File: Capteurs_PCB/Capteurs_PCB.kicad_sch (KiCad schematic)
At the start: 0 parts

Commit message: update kicad
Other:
- sheet Regulation 5V renamed Regulation
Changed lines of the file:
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@@
     (stroke (width 0.1524) (type solid))
     (fill (color 0 0 0 0.0000))
-    (property "Sheetname" "Regulation 5V" (at 25.4 72.9484 0)
+    (property "Sheetname" "Regulation" (at 25.4 72.9484 0)
       (effects (font (size 1.27 1.27)) (justify left bottom))
     )

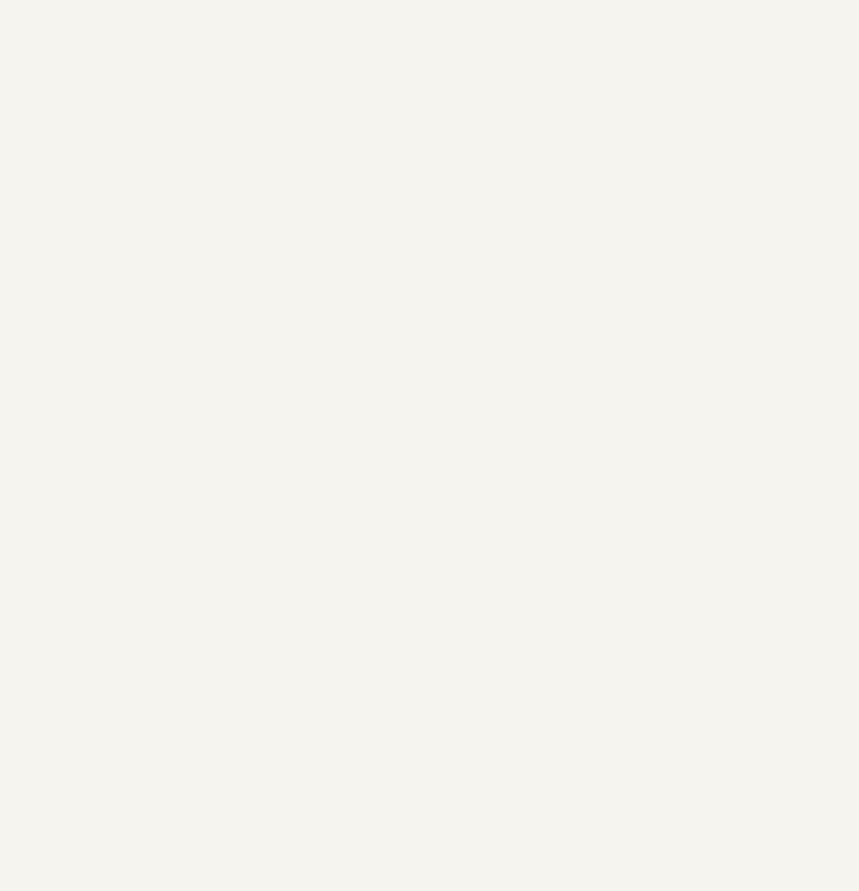
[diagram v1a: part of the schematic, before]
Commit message: PCB changement
Pcb changé (Raspberry))
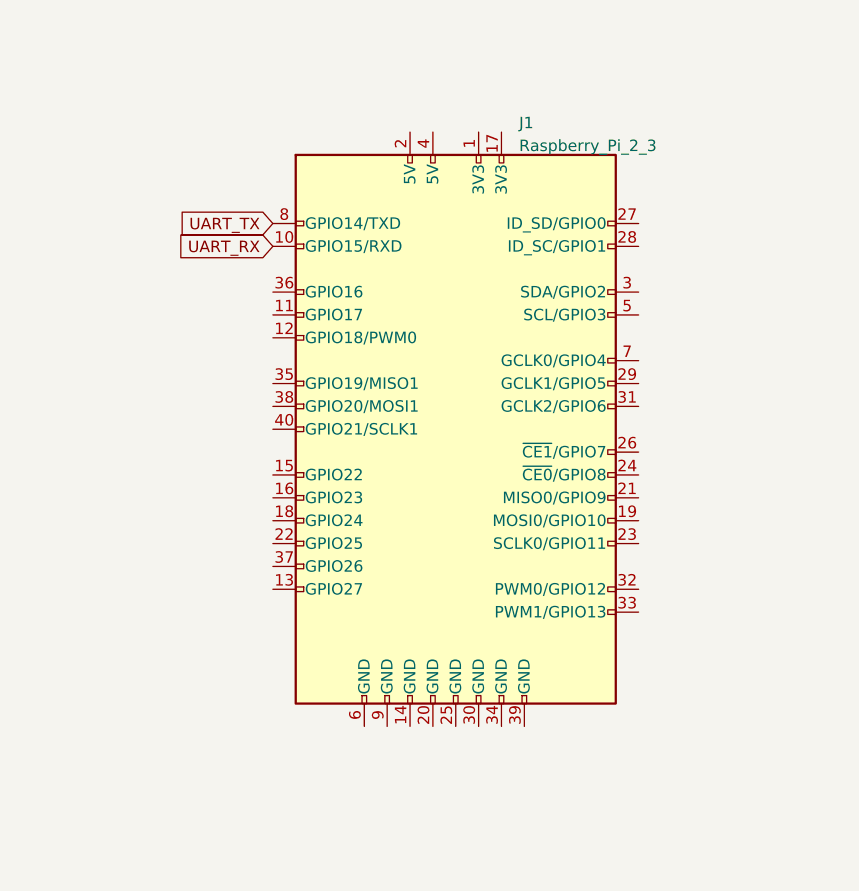
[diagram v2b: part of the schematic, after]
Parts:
- added J1: Raspberry_Pi_2_3, symbol Connector:Raspberry_Pi_2_3
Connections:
- new net UART_RX: J1.10 (GPIO15/RXD)
- new net UART_TX: J1.8 (GPIO14/TXD)
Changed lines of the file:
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@@
     (title "PCB_CAPTEUR_ALIM")
+  )
+  (global_label "UART_TX" (shape input) (at 105.156 42.926 180) (fields_autoplaced)
+    (effects (font (size 1.27 1.27)) (justify right))
+    (property "Intersheetrefs" "${INTERSHEET_REFS}" (at 94.4488 42.926 0)
+      (effects (font (size 1.27 1.27)) (justify right) hide)
+    )
+  )
+  (global_label "UART_RX" (shape input) (at 105.156 45.466 180) (fields_autoplaced)
+    (effects (font (size 1.27 1.27)) (justify right))
+    (property "Intersheetrefs" "${INTERSHEET_REFS}" (at 94.1464 45.466 0)
+      (effects (font (size 1.27 1.27)) (justify right) hide)
+    )
+  )
+  (symbol (lib_id "Connector:Raspberry_Pi_2_3") (at 125.476 65.786 0) (unit 1)
+    (in_bom yes) (on_board yes) (dnp no) (fields_autoplaced)
+    (property "Reference" "J1" (at 132.5119 31.75 0)
+      (effects (font (size 1.27 1.27)) (justify left))
+    )
+    (property "Value" "Raspberry_Pi_2_3" (at 132.5119 34.29 0)
+      (effects (font (size 1.27 1.27)) (justify left))
+    )
+    (property "Footprint" "" (at 125.476 65.786 0)
+      (effects (font (size 1.27 1.27)) hide)
+    )
+    (property "Datasheet" "https://www.raspberrypi.org/documentation/hardware/raspberrypi/schematics/rpi_SCH_3bplus_1p0_reduced.pdf" (at 125.476 65.786 0)
+      (effects (font (size 1.27 1.27)) hide)
+    )
+    (pin "1")
+    (pin "10")
+    (pin "11")
+    (pin "12")
+    (pin "13")
+    (pin "14")
+    (pin "15")
+    (pin "16")
+    (pin "17")
+    (pin "18")
+    (pin "19")
+    (pin "2")
+    (pin "20")
+    (pin "21")
+    (pin "22")
+    (pin "23")
+    (pin "24")
+    (pin "25")
+    (pin "26")
+    (pin "27")
+    (pin "28")
+    (pin "29")
+    (pin "3")
+    (pin "30")
+    (pin "31")
+    (pin "32")
+    (pin "33")
+    (pin "34")
+    (pin "35")
+    (pin "36")
+    (pin "37")
+    (pin "38")
+    (pin "39")
+    (pin "4")
+    (pin "40")
+    (pin "5")
+    (pin "6")
+    (pin "7")
+    (pin "8")
+    (pin "9")
+    (instances
+      (project "Capteurs_PCB"
+        (path "/1101af8f-9425-4102-9245-339dc54562bf"
+          (reference "J1") (unit 1)
+        )
+      )
+    )
   )
   (sheet (at 24.13 130.81) (size 64.77 53.34) (fields_autoplaced)

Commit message: pcb update
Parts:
- removed J1: Raspberry_Pi_2_3, symbol Connector:Raspberry_Pi_2_3
- added J1: Batterie, symbol Connector:Conn_01x02_Socket
- added J2: RaspberryPi, symbol Connector:Conn_01x02_Socket
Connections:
- net UART_RX: now also J2.2 (Pin_2)
- net UART_TX: now also J2.1 (Pin_1)
- new net Earth: J1.1 (Pin_1)
- new net VBATTERIE: J1.2 (Pin_2)
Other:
- note added: "Batterie"
- note added: "Branchement RaspberryPi"

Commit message: uptdate PCB
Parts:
- added J3: Prop1, symbol Connector:Conn_01x03_Pin
- added J4: Prop2, symbol Connector:Conn_01x03_Pin
- added J5: Alim_Prop1, symbol Connector:Conn_01x02_Socket
- added J6: Alim_Prop2, symbol Connector:Conn_01x02_Socket
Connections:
- net Earth: now also J3.3 (Pin_3), J4.3 (Pin_3), J5.2 (Pin_2), J6.2 (Pin_2)
- new net 5_V5: J3.2 (Pin_2), J4.2 (Pin_2)
- new net SigProp1: J3.1 (Pin_1)
- new net SigProp2: J4.1 (Pin_1)
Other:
- note added: "Propulseurs"
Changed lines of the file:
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@@
   (junction (at 64.77 81.28) (diameter 0) (color 0 0 0 0)
   )
+  (junction (at 91.44 74.93) (diameter 0) (color 0 0 0 0)
+  )
   (junction (at 111.76 128.27) (diameter 0) (color 0 0 0 0)
   )
@@
     (stroke (width 0) (type default))
   )
+  (wire (pts (xy 91.44 74.93) (xy 91.44 77.47))
+    (stroke (width 0) (type default))
+  )
+  (wire (pts (xy 87.63 77.47) (xy 87.63 74.93))
+    (stroke (width 0) (type default))
+  )
   (wire (pts (xy 104.14 132.08) (xy 116.84 132.08))
     (stroke (width 0) (type default))
@@
     (stroke (width 0) (type default))
   )
+  (wire (pts (xy 87.63 74.93) (xy 91.44 74.93))
+    (stroke (width 0) (type default))
+  )
   (wire (pts (xy 104.14 96.52) (xy 116.84 96.52))
     (stroke (width 0) (type default))
@@
     (stroke (width 0) (type default))
   )
-  (wire (pts (xy 91.44 67.31) (xy 91.44 77.47))
+  (wire (pts (xy 91.44 67.31) (xy 91.44 74.93))
     (stroke (width 0) (type default))
   )
@@
   (wire (pts (xy 64.77 81.28) (xy 64.77 67.31))
     (stroke (width 0) (type default))
+  )
+  (rectangle (start 212.09 45.72) (end 265.43 96.52)
+    (stroke (width 0) (type default))
+    (fill (type none))
   )
   (rectangle (start 63.5 24.13) (end 90.17 52.07)
@@
     (effects (font (size 1.27 1.27)) (justify left bottom))
   )
+  (text "Propulseurs\n" (at 212.09 45.72 0)
+    (effects (font (size 1.27 1.27)) (justify left bottom))
+  )
   (global_label "V_5V" (shape input) (at 53.34 85.09 180) (fields_autoplaced)
     (effects (font (size 1.27 1.27)) (justify right))
@@
     )
   )
+  (global_label "SigProp1" (shape input) (at 226.06 57.15 180) (fields_autoplaced)
+    (effects (font (size 1.27 1.27)) (justify right))
+    (property "Intersheetrefs" "${INTERSHEET_REFS}" (at 214.6272 57.15 0)
+      (effects (font (size 1.27 1.27)) (justify right) hide)
+    )
+  )
   (global_label "SDX" (shape input) (at 116.84 87.63 0) (fields_autoplaced)
     (effects (font (size 1.27 1.27)) (justify left))
@@
     )
   )
+  (global_label "5_V5" (shape input) (at 226.06 54.61 180) (fields_autoplaced)
+    (effects (font (size 1.27 1.27)) (justify right))
+    (property "Intersheetrefs" "${INTERSHEET_REFS}" (at 218.679 54.61 0)
+      (effects (font (size 1.27 1.27)) (justify right) hide)
+    )
+  )
   (global_label "INT2" (shape input) (at 104.14 99.06 180) (fields_autoplaced)
     (effects (font (size 1.27 1.27)) (justify right))
@@
     )
   )
+  (global_label "SigProp2" (shape input) (at 226.06 67.31 180) (fields_autoplaced)
+    (effects (font (size 1.27 1.27)) (justify right))
+    (property "Intersheetrefs" "${INTERSHEET_REFS}" (at 214.6272 67.31 0)
+      (effects (font (size 1.27 1.27)) (justify right) hide)
+    )
+  )
   (global_label "CS" (shape input) (at 116.84 90.17 0) (fields_autoplaced)
     (effects (font (size 1.27 1.27)) (justify left))
@@
     )
   )
+  (global_label "5_V5" (shape input) (at 226.06 64.77 180) (fields_autoplaced)
+    (effects (font (size 1.27 1.27)) (justify right))
+    (property "Intersheetrefs" "${INTERSHEET_REFS}" (at 218.679 64.77 0)
+      (effects (font (size 1.27 1.27)) (justify right) hide)
+    )
+  )
   (global_label "SS" (shape input) (at 104.14 139.7 180) (fields_autoplaced)
     (effects (font (size 1.27 1.27)) (justify right))
@@
         (path "/1101af8f-9425-4102-9245-339dc54562bf"
           (reference "J1") (unit 1)
+        )
+      )
+    )
+  )
+  (symbol (lib_id "Connector:Conn_01x02_Socket") (at 231.14 83.82 0) (unit 1)
+    (in_bom yes) (on_board yes) (dnp no)
+    (property "Reference" "J6" (at 231.14 92.71 0)
+      (effects (font (size 1.27 1.27)))
+    )
+    (property "Value" "Alim_Prop2" (at 231.14 90.17 0)
+      (effects (font (size 1.27 1.27)))
+    )
+    (property "Footprint" "" (at 231.14 83.82 0)
+      (effects (font (size 1.27 1.27)) hide)
+    )
+    (property "Datasheet" "~" (at 231.14 83.82 0)
+      (effects (font (size 1.27 1.27)) hide)
+    )
+    (pin "1")
+    (pin "2")
+    (instances
+      (project "Capteurs_PCB"
+        (path "/1101af8f-9425-4102-9245-339dc54562bf"
+          (reference "J6") (unit 1)
+        )
+      )
+    )
+  )
+  (symbol (lib_id "power:Earth") (at 226.06 52.07 270) (unit 1)
+    (in_bom yes) (on_board yes) (dnp no) (fields_autoplaced)
+    (property "Reference" "#PWR09" (at 219.71 52.07 0)
+      (effects (font (size 1.27 1.27)) hide)
+    )
+    (property "Value" "Earth" (at 222.25 52.07 0)
+      (effects (font (size 1.27 1.27)) hide)
+    )
+    (property "Footprint" "" (at 226.06 52.07 0)
+      (effects (font (size 1.27 1.27)) hide)
+    )
+    (property "Datasheet" "~" (at 226.06 52.07 0)
+      (effects (font (size 1.27 1.27)) hide)
+    )
+    (pin "1")
+    (instances
+      (project "Capteurs_PCB"
+        (path "/1101af8f-9425-4102-9245-339dc54562bf"
+          (reference "#PWR09") (unit 1)
         )
       )
@@
     )
   )
+  (symbol (lib_id "power:Earth") (at 226.06 74.93 270) (unit 1)
+    (in_bom yes) (on_board yes) (dnp no) (fields_autoplaced)
+    (property "Reference" "#PWR011" (at 219.71 74.93 0)
+      (effects (font (size 1.27 1.27)) hide)
+    )
+    (property "Value" "Earth" (at 222.25 74.93 0)
+      (effects (font (size 1.27 1.27)) hide)
+    )
+    (property "Footprint" "" (at 226.06 74.93 0)
+      (effects (font (size 1.27 1.27)) hide)
+    )
+    (property "Datasheet" "~" (at 226.06 74.93 0)
+      (effects (font (size 1.27 1.27)) hide)
+    )
+    (pin "1")
+    (instances
+      (project "Capteurs_PCB"
+        (path "/1101af8f-9425-4102-9245-339dc54562bf"
+          (reference "#PWR011") (unit 1)
+        )
+      )
+    )
+  )
+  (symbol (lib_id "Connector:Conn_01x03_Pin") (at 231.14 54.61 180) (unit 1)
+    (in_bom yes) (on_board yes) (dnp no) (fields_autoplaced)
+    (property "Reference" "J3" (at 232.41 53.975 0)
+      (effects (font (size 1.27 1.27)) (justify right))
+    )
+    (property "Value" "Prop1" (at 232.41 56.515 0)
+      (effects (font (size 1.27 1.27)) (justify right))
+    )
+    (property "Footprint" "" (at 231.14 54.61 0)
+      (effects (font (size 1.27 1.27)) hide)
+    )
+    (property "Datasheet" "~" (at 231.14 54.61 0)
+      (effects (font (size 1.27 1.27)) hide)
+    )
+    (pin "1")
+    (pin "2")
+    (pin "3")
+    (instances
+      (project "Capteurs_PCB"
+        (path "/1101af8f-9425-4102-9245-339dc54562bf"
+          (reference "J3") (unit 1)
+        )
+      )
+    )
+  )
+  (symbol (lib_id "power:Earth") (at 226.06 86.36 270) (unit 1)
+    (in_bom yes) (on_board yes) (dnp no) (fields_autoplaced)
+    (property "Reference" "#PWR012" (at 219.71 86.36 0)
+      (effects (font (size 1.27 1.27)) hide)
+    )
+    (property "Value" "Earth" (at 222.25 86.36 0)
+      (effects (font (size 1.27 1.27)) hide)
+    )
+    (property "Footprint" "" (at 226.06 86.36 0)
+      (effects (font (size 1.27 1.27)) hide)
+    )
+    (property "Datasheet" "~" (at 226.06 86.36 0)
+      (effects (font (size 1.27 1.27)) hide)
+    )
+    (pin "1")
+    (instances
+      (project "Capteurs_PCB"
+        (path "/1101af8f-9425-4102-9245-339dc54562bf"
+          (reference "#PWR012") (unit 1)
+        )
+      )
+    )
+  )
   (symbol (lib_id "power:Earth") (at 34.29 55.88 0) (unit 1)
     (in_bom yes) (on_board yes) (dnp no) (fields_autoplaced)
@@
         )
       )
+    )
+  )
+  (symbol (lib_id "power:Earth") (at 226.06 62.23 270) (unit 1)
+    (in_bom yes) (on_board yes) (dnp no) (fields_autoplaced)
+    (property "Reference" "#PWR010" (at 219.71 62.23 0)
+      (effects (font (size 1.27 1.27)) hide)
+    )
+    (property "Value" "Earth" (at 222.25 62.23 0)
+      (effects (font (size 1.27 1.27)) hide)
+    )
+    (property "Footprint" "" (at 226.06 62.23 0)
+      (effects (font (size 1.27 1.27)) hide)
+    )
+    (property "Datasheet" "~" (at 226.06 62.23 0)
+      (effects (font (size 1.27 1.27)) hide)
+    )
+    (pin "1")
+    (instances
+      (project "Capteurs_PCB"
+        (path "/1101af8f-9425-4102-9245-339dc54562bf"
+          (reference "#PWR010") (unit 1)
+        )
+      )
+    )
+  )
+  (symbol (lib_id "Connector:Conn_01x03_Pin") (at 231.14 64.77 180) (unit 1)
+    (in_bom yes) (on_board yes) (dnp no) (fields_autoplaced)
+    (property "Reference" "J4" (at 232.41 64.135 0)
+      (effects (font (size 1.27 1.27)) (justify right))
+    )
+    (property "Value" "Prop2" (at 232.41 66.675 0)
+      (effects (font (size 1.27 1.27)) (justify right))
+    )
+    (property "Footprint" "" (at 231.14 64.77 0)
+      (effects (font (size 1.27 1.27)) hide)
+    )
+    (property "Datasheet" "~" (at 231.14 64.77 0)
+      (effects (font (size 1.27 1.27)) hide)
+    )
+    (pin "1")
+    (pin "2")
+    (pin "3")
+    (instances
+      (project "Capteurs_PCB"
+        (path "/1101af8f-9425-4102-9245-339dc54562bf"
+          (reference "J4") (unit 1)
+        )
+      )
+    )
+  )
+  (symbol (lib_id "Connector:Conn_01x02_Socket") (at 231.14 72.39 0) (unit 1)
+    (in_bom yes) (on_board yes) (dnp no)
+    (property "Reference" "J5" (at 231.14 81.28 0)
+      (effects (font (size 1.27 1.27)))
+    )
+    (property "Value" "Alim_Prop1" (at 231.14 78.74 0)
+      (effects (font (size 1.27 1.27)))
+    )
+    (property "Footprint" "" (at 231.14 72.39 0)
+      (effects (font (size 1.27 1.27)) hide)
+    )
+    (property "Datasheet" "~" (at 231.14 72.39 0)
+      (effects (font (size 1.27 1.27)) hide)
+    )
+    (pin "1")
+    (pin "2")
+    (instances
+      (project "Capteurs_PCB"
+        (path "/1101af8f-9425-4102-9245-339dc54562bf"
+          (reference "J5") (unit 1)
+        )
+      )

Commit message: updates pcb
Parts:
- added J7: Moteur_seringues_1, Connector_PinSocket_2.54mm:PinSocket_1x02_P2.54mm_Vertical, symbol Connector:Conn_01x02_Socket
- added J8: Moteur_seringues_2, Connector_PinSocket_2.54mm:PinSocket_1x02_P2.54mm_Vertical, symbol Connector:Conn_01x02_Socket
- added J9: LED, Connector_PinHeader_2.54mm:PinHeader_1x04_P2.54mm_Vertical, symbol Connector:Conn_01x04_Pin
- added U7, U8: ZXBM5210-SP, Package_SO:Diodes_SO-8EP, symbol Driver_Motor:ZXBM5210-SP
- J2: footprint (none) -> Connector_PinSocket_2.54mm:PinSocket_1x02_P2.54mm_Vertical
- J3, J4: footprint (none) -> Connector_PinHeader_2.54mm:PinHeader_1x03_P2.54mm_Vertical
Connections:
- net Earth: now also J9.2 (Pin_2), J9.4 (Pin_4), U7.8 (GND), U7.9 (GND), U8.8 (GND), U8.9 (GND)
- net V_12V: now also J5.1 (Pin_1), J6.1 (Pin_1), U7.2 (VM), U7.3 (VDD), U7.6 (VREF), U8.2 (VM), U8.3 (VDD), U8.6 (VREF)
- net 5_V5 renamed VDD_LED
- net VDD_LED: now also J9.3 (Pin_3)
- new net: J8.1 (Pin_1), U8.1 (OUT1)
- new net: J8.2 (Pin_2), U8.7 (OUT2)
- new net: J7.1 (Pin_1), U7.1 (OUT1)
- new net: J7.2 (Pin_2), U7.7 (OUT2)
- new net FWD1: U7.4 (FWD)
- new net FWD2: U8.4 (FWD)
- new net REV1: U7.5 (REV)
- new net REV2: U8.5 (REV)
- new net Sig_LED: J9.1 (Pin_1)
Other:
- note added: "LED"
- note added: "Moteurs seringues"
- title: PCB_CAPTEUR_ALIM -> PCB_SOUS-MARIN
- moved on the sheet: J3, J4, J5, J6

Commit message: Modif seringues pcb
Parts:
- J1: footprint (none) -> Connector_PinSocket_2.54mm:PinSocket_1x02_P2.54mm_Vertical
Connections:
- net VBATTERIE: now also U7.2 (VM), U7.3 (VDD), U7.6 (VREF), U8.2 (VM), U8.3 (VDD), U8.6 (VREF)
- net V_12V: no longer U7.2 (VM), U7.3 (VDD), U7.6 (VREF), U8.2 (VM), U8.3 (VDD), U8.6 (VREF)
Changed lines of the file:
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@@
   (junction (at 64.77 81.28) (diameter 0) (color 0 0 0 0)
   )
+  (junction (at 39.37 66.04) (diameter 0) (color 0 0 0 0)
+  )
   (junction (at 213.36 127) (diameter 0) (color 0 0 0 0)
   )
@@
   (junction (at 91.44 74.93) (diameter 0) (color 0 0 0 0)
   )
-  (junction (at 55.88 88.9) (diameter 0) (color 0 0 0 0)
-  )
   (junction (at 111.76 128.27) (diameter 0) (color 0 0 0 0)
   )
@@
     (stroke (width 0) (type default))
   )
-  (wire (pts (xy 53.34 85.09) (xy 63.5 85.09))
+  (wire (pts (xy 53.34 85.09) (xy 62.23 85.09))
     (stroke (width 0) (type default))
   )
@@
     (stroke (width 0) (type default))
   )
-  (wire (pts (xy 59.69 88.9) (xy 59.69 104.14))
-    (stroke (width 0) (type default))
-  )
   (wire (pts (xy 104.14 90.17) (xy 116.84 90.17))
     (stroke (width 0) (type default))
   )
-  (wire (pts (xy 39.37 53.34) (xy 39.37 73.66))
+  (wire (pts (xy 39.37 53.34) (xy 39.37 66.04))
     (stroke (width 0) (type default))
   )
@@
     (stroke (width 0) (type default))
   )
-  (wire (pts (xy 63.5 85.09) (xy 63.5 104.14))
+  (wire (pts (xy 62.23 85.09) (xy 62.23 104.14))
     (stroke (width 0) (type default))
   )
@@
     (stroke (width 0) (type default))
   )
-  (wire (pts (xy 55.88 88.9) (xy 59.69 88.9))
-    (stroke (width 0) (type default))
-  )
   (wire (pts (xy 91.44 120.65) (xy 91.44 110.49))
     (stroke (width 0) (type default))
@@
     (stroke (width 0) (type default))
   )
+  (wire (pts (xy 44.45 66.04) (xy 39.37 66.04))
+    (stroke (width 0) (type default))
+  )
   (wire (pts (xy 104.14 87.63) (xy 116.84 87.63))
     (stroke (width 0) (type default))
@@
   )
   (wire (pts (xy 111.76 102.87) (xy 111.76 128.27))
+    (stroke (width 0) (type default))
+  )
+  (wire (pts (xy 39.37 66.04) (xy 39.37 73.66))
     (stroke (width 0) (type default))
   )
@@
     )
   )
+  (global_label "V_ALIM_SER" (shape input) (at 44.45 66.04 0) (fields_autoplaced)
+    (effects (font (size 1.27 1.27)) (justify left))
+    (property "Intersheetrefs" "${INTERSHEET_REFS}" (at 58.181 66.04 0)
+      (effects (font (size 1.27 1.27)) (justify left) hide)
+    )
+  )
   (global_label "V_5V" (shape input) (at 224.79 39.37 180) (fields_autoplaced)
     (effects (font (size 1.27 1.27)) (justify right))
@@
     )
   )
-  (global_label "V_ALIM_SER" (shape input) (at 59.69 104.14 270) (fields_autoplaced)
-    (effects (font (size 1.27 1.27)) (justify right))
-    (property "Intersheetrefs" "${INTERSHEET_REFS}" (at 59.69 117.871 90)
-      (effects (font (size 1.27 1.27)) (justify right) hide)
-    )
-  )
   (global_label "V_ALIM_PROP" (shape input) (at 224.79 57.15 180) (fields_autoplaced)
     (effects (font (size 1.27 1.27)) (justify right))
@@
     )
   )
-  (global_label "VDD_LED" (shape input) (at 63.5 104.14 270) (fields_autoplaced)
-    (effects (font (size 1.27 1.27)) (justify right))
-    (property "Intersheetrefs" "${INTERSHEET_REFS}" (at 63.5 115.0891 90)
+  (global_label "VDD_LED" (shape input) (at 62.23 104.14 270) (fields_autoplaced)
+    (effects (font (size 1.27 1.27)) (justify right))
+    (property "Intersheetrefs" "${INTERSHEET_REFS}" (at 62.23 115.0891 90)
       (effects (font (size 1.27 1.27)) (justify right) hide)
     )
@@
       (effects (font (size 1.27 1.27)))
     )
-    (property "Footprint" "" (at 29.21 55.88 0)
+    (property "Footprint" "Connector_PinSocket_2.54mm:PinSocket_1x02_P2.54mm_Vertical" (at 29.21 55.88 0)
       (effects (font (size 1.27 1.27)) hide)
     )

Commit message: modif kicad
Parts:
- J1: footprint Connector_PinSocket_2.54mm:PinSocket_1x02_P2.54mm_Vertical -> Connector_Hirose:Hirose_DF13-02P-1.25DSA_1x02_P1.25mm_Vertical
- J5, J6: footprint (none) -> Connector_Hirose:Hirose_DF13-02P-1.25DSA_1x02_P1.25mm_Vertical
